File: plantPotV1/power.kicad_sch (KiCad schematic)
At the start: 0 parts

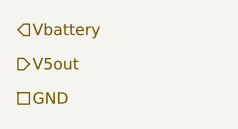
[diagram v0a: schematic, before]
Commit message: updated circuit diagram (top only)
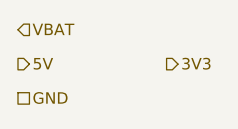
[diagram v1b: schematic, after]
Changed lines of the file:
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@@
 		(comment 4 "Stanford University")
 	)
-	(hierarchical_label "V5out"
+	(hierarchical_label "5V"
 		(shape output)
 		(at 138.43 105.41 0)
@@
 		)
 	)
-	(hierarchical_label "Vbattery"
+	(hierarchical_label "3V3"
+		(shape output)
+		(at 154.94 105.41 0)
+		(fields_autoplaced yes)
+		(effects
+			(font
+				(size 1.27 1.27)
+			)
+			(justify left)
+		)
+	)
+	(hierarchical_label "VBAT"
 		(shape input)
 		(at 138.43 101.6 0)
